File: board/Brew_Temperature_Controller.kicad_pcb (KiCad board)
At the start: 2 copper layers, 55.9 x 53.3 mm, 12 parts, among them J1 Conn_01x04_Male, J2 Screw_Terminal_01x02, J3 Conn_01x02_Male, Q1 IRLU024NPBF, SW1 SW_Push, SW2 SW_Push, U1 Nokia_5110_Module

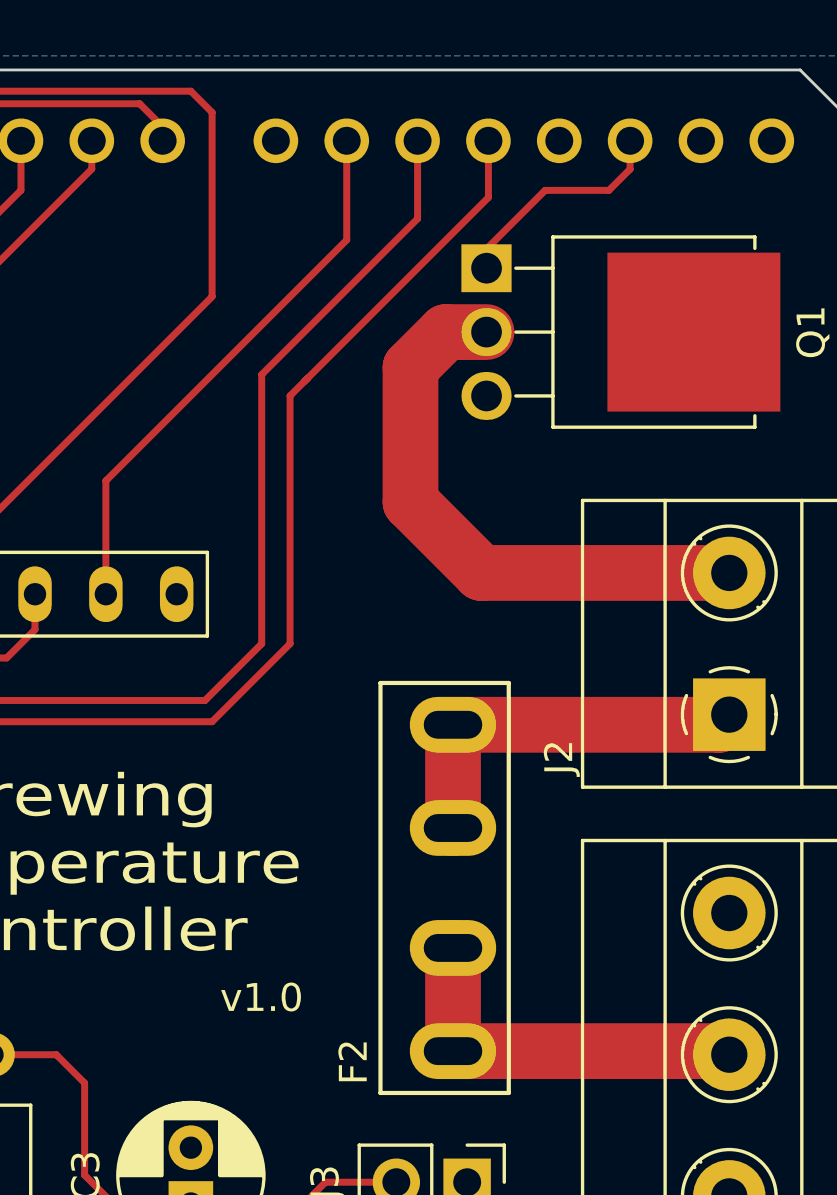
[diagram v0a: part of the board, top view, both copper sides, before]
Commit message: Board tweaks and software update
The use of D2 to control the heater was a mistake as it does not
provide PWM, switch to using D3.

The chosen MOSFET was not suitable for driving the heater at full
current and has thus been switched for a more powerful one.

Move the README so that it's more general for the whole project rather
than just the board design and use Markdown.

Add license to source code.

Add features to the software:

- Drive output with PWM
- Utilise screen backlight
- Save set temperature across boots
- Display percentage power output when on
- Test for detached thermistor and turn off output as safety measure
- Allow scrolling of setpoint with long press of buttons
- Log to serial at approx 1Hz

Signed-off-by: Martyn Welch <martyn.welch@collabora.com>
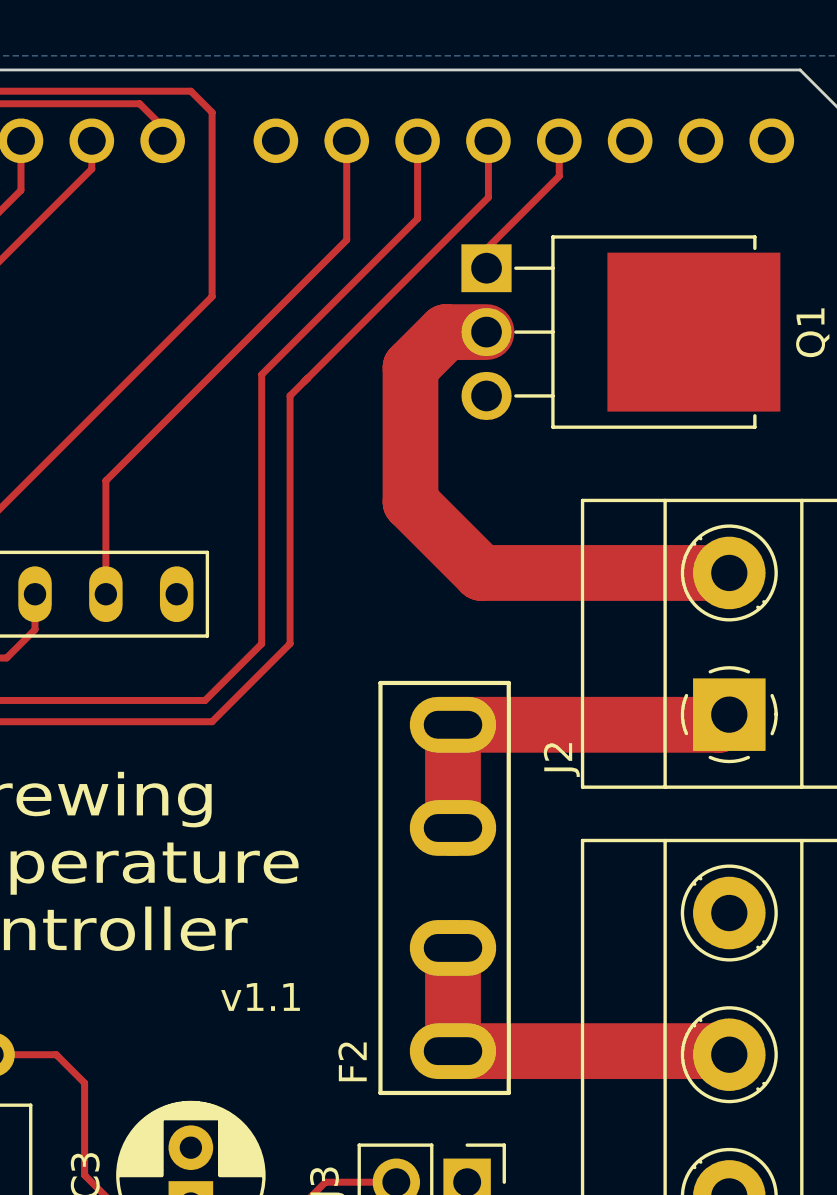
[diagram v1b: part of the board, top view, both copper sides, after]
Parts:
- F1, F2: value Fuse -> MCCQ-122
- J1: value Conn_01x04_Male -> CTBP9358/4
- J2: value Screw_Terminal_01x02 -> CTB0708/2
- SW1, SW2: value SW_Push -> MCDTS6-1R
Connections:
- A1 pad 17: HEATER -> (no net)
- A1 pad 18: (no net) -> HEATER
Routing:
- net HEATER: track 8.04 -> 5.65 mm
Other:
- board text added: "v1.1"
- board text removed: "v1.0"
